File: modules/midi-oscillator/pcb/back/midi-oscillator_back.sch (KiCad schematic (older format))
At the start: 17 parts, among them J1 DEBUG, J2 Conn_02x08_Odd_Even, J3 Conn_01x14, U1 Pico, U2 MCP4822, U3 MCP4822, U4 24LC512

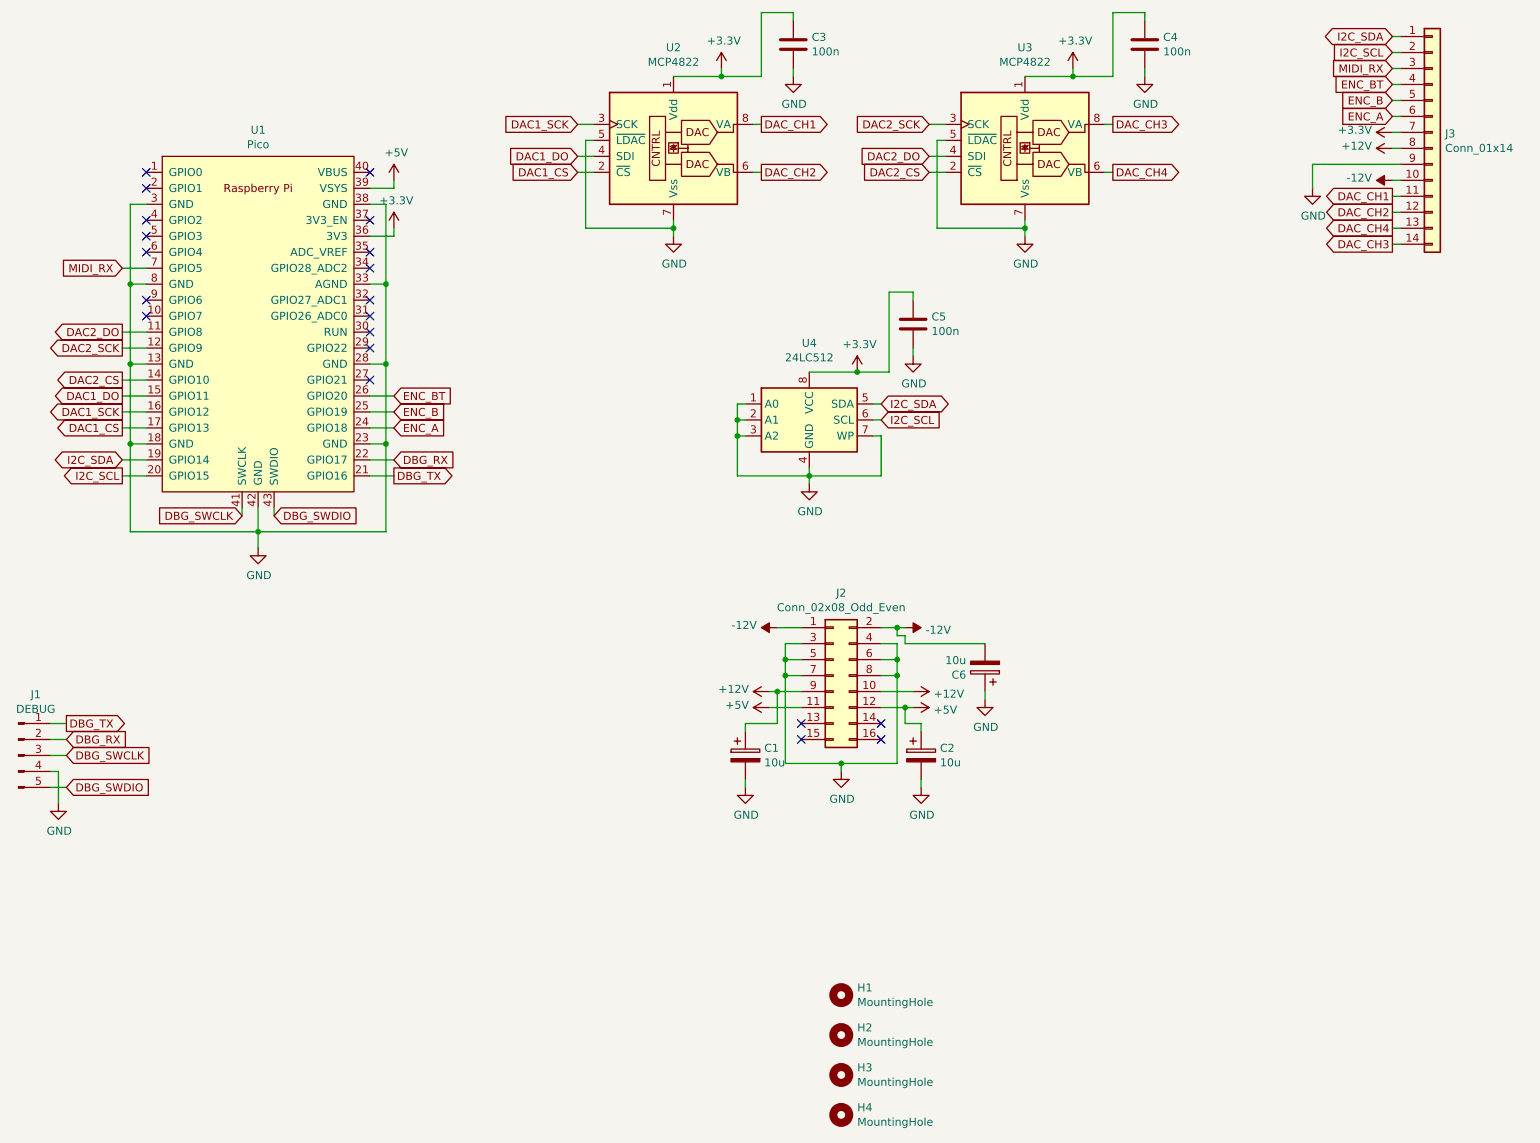
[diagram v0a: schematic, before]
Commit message: modules: midi-oscilator: pcb: fix schematics and add page metadata
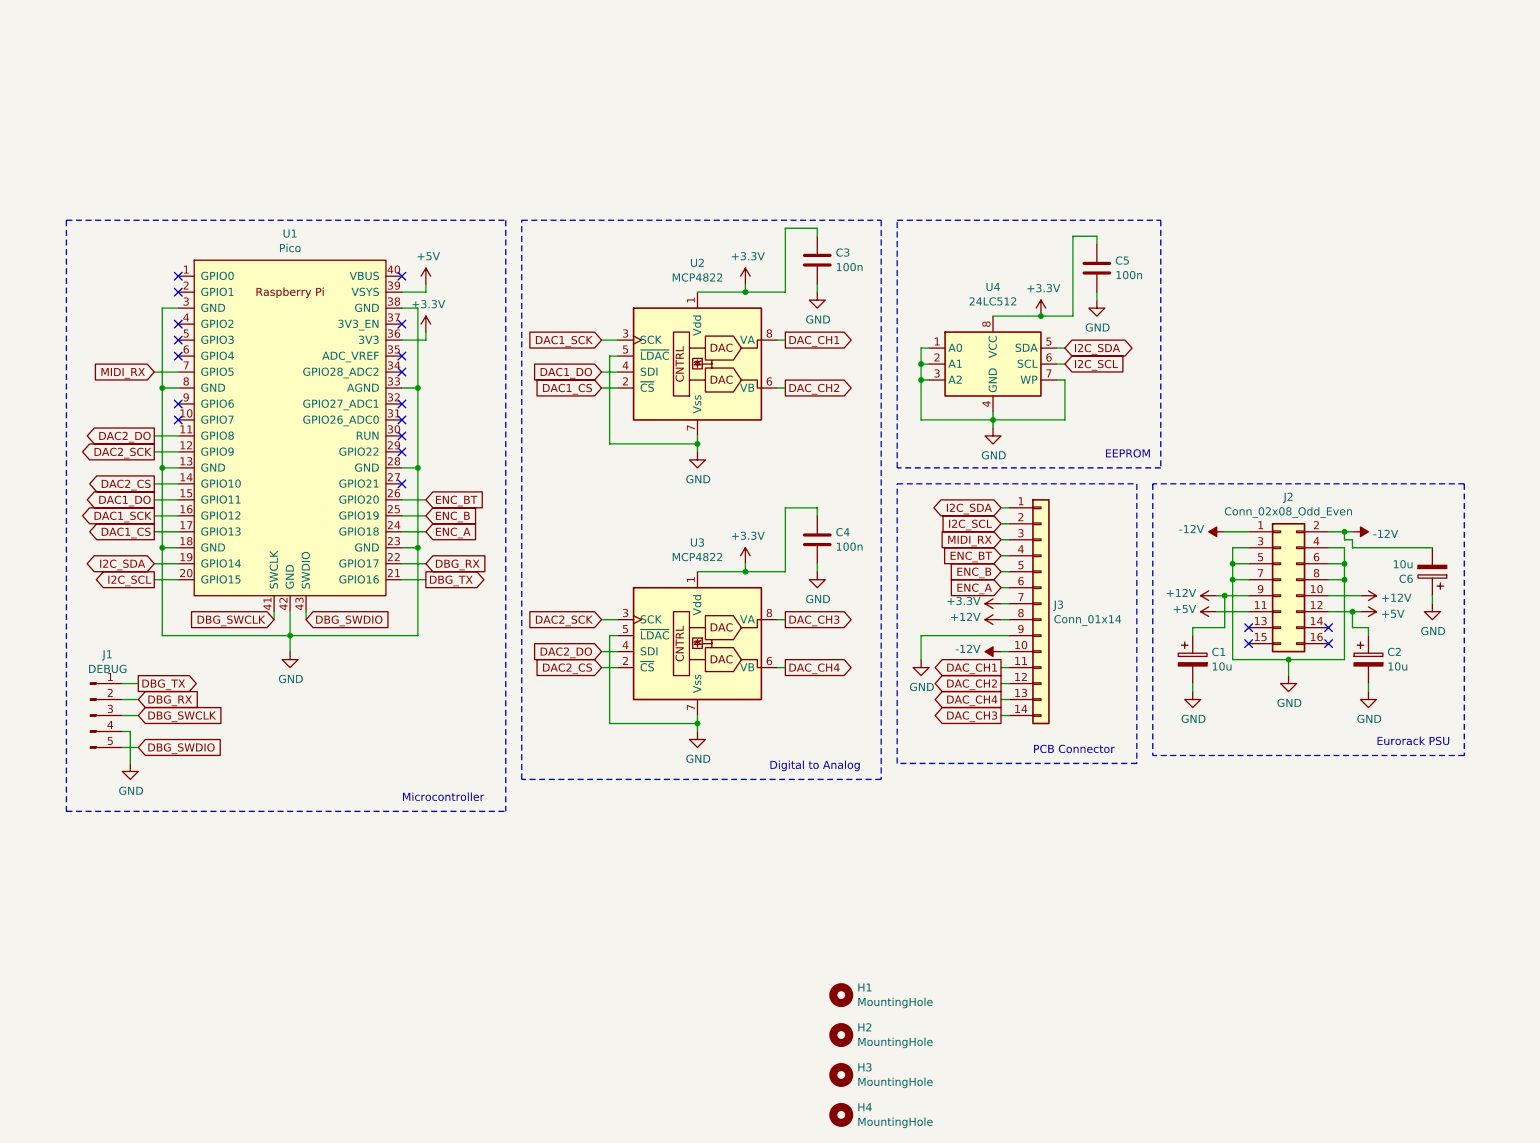
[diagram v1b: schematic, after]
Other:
- note added: "Digital to Analog"
- note added: "EEPROM"
- note added: "Eurorack PSU"
- note added: "Microcontroller"
- note added: "PCB Connector"
- moved on the sheet: C1, C2, C3, C4, C5, C6, J1, J2, J3, U1, U2, U3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

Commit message: modules: midi-oscillator: schematic improvements, added pdf
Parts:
- J1: value DEBUG -> JST XH 1x5; symbol Connector:Conn_01x05_Male -> Connector_Generic:Conn_01x05
- J2: value Conn_02x08_Odd_Even -> IDC Header 2x8
- J3: value Conn_01x14 -> Pin Socket 1x14
- U1: value Pico -> Raspberry Pi Pico
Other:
- moved on the sheet: C3, J3, U2
